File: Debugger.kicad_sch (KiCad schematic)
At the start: 32 parts, among them IC1 STM32F103C8T6, J1 USB_B_Micro, J2 Conn_01x06_Pin, Q4 MMBT3904, SW1 RESET, U4 USBLC6-2SC6, Y1 8MHz

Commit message: update
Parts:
- SW1: value RESET -> SW_Push
- renumbered IC1 to U6
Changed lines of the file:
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@@
 		(on_board yes)
 		(dnp no)
-		(property "Reference" "IC1"
+		(property "Reference" "U6"
 			(at 124.968 102.362 0)
 			(effects
@@
 			(project ""
 				(path "/c703575f-b97a-4282-ae81-d5777b8a5a01/7972b3b3-0781-42c8-aedd-35cecbf74189"
-					(reference "IC1")
+					(reference "U6")
 					(unit 1)
 				)
@@
 			)
 		)
-		(property "Value" "RESET"
+		(property "Value" "SW_Push"
 			(at 237.49 48.2599 90)
 			(effects

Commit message: Done ERC + Documentation
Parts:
- removed Q4: MMBT3904, Package_TO_SOT_SMD:SOT-23, symbol Simulation_SPICE:NPN
- removed R45: 36k, Resistor_SMD:R_0603_1608Metric, symbol Device:R_US
- removed R46: 100k, Resistor_SMD:R_0603_1608Metric, symbol Device:R_US
- added R23, R24: 22R, Resistor_SMD:R_0603_1608Metric, symbol Device:R_US
- U3: renamed from U6; footprint QFP50P900X900X160-48N -> footprints:QFP50P900X900X160-48N; MPN (none) -> STM32F103C8T6; Manufacturer_Part_Number STM32F103C8T6 -> (none)
- U4: MPN (none) -> USBLC6-2SC6
- renumbered C1 to C21, C2 to C22, C3 to C23, C4 to C24, C5 to C25, C6 to C26, C7 to C27, C8 to C28, C9 to C29, C10 to C30, D1 to D6, D2 to D7, J2 to J4, J1 to J5, R1 to R15, R2 to R16, R3 to R17, R4 to R18, R5 to R19, R6 to R20, R7 to R21, R8 to R22, R9 to R25, R44 to R26, R10 to R27, SW1 to SW5
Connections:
- net +3.3V: now also R26.1
- net USB_DN: now also R24.1; no longer U4.3 (I/O2)
- net USB_DP: now also R23.2; no longer R26.2, U4.1 (I/O1)
- net T_NRST renamed RESET
- new net: R23.1, R26.2, U4.1 (I/O1)
- new net: R24.2, U4.3 (I/O2)
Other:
- moved on the sheet: D7, J5, R26, R27, U4

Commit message: Initial Review Changes
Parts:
- added F1: Polyfuse, Fuse:Fuse_1206_3216Metric, symbol Device:Polyfuse
- J4: value Conn_01x06_Pin -> F103 SWD
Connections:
- net at D7.2 (A), U4.5 (VBUS): now also F1.1; no longer J5.1 (VBUS)
- new net: F1.2, J5.1 (VBUS)
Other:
- company: (none) -> _electronic_projects
- title: (none) -> DeskNode-F4
- moved on the sheet: J5
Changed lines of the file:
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@@
 	(generator_version "9.0")
 	(paper "A4")
+	(title_block
+		(title "DeskNode-F4")
+		(rev "A")
+		(company "_electronic_projects")
+		(comment 1 "Wajahatulla Sharif")
+		(comment 2 "Designed by ")
+	)
 	(rectangle
 		(start 218.186 125.73)
@@
 	)
 	(junction
-		(at 254 95.25)
+		(at 69.85 114.3)
 		(diameter 0)
 		(color 0 0 0 0)
 	)
 	(junction
-		(at 69.85 114.3)
+		(at 270.51 114.3)
 		(diameter 0)
 		(color 0 0 0 0)
@@
 	)
 	(junction
-		(at 267.97 114.3)
-		(diameter 0)
-		(color 0 0 0 0)
-	)
-	(junction
 		(at 257.81 114.3)
 		(diameter 0)
@@
 	)
 	(junction
+		(at 254 95.25)
+		(diameter 0)
+		(color 0 0 0 0)
+	)
+	(junction
 		(at 78.74 48.26)
 		(diameter 0)
@@
 	(wire
 		(pts
-			(xy 254 95.25) (xy 260.35 95.25)
-		)
-		(stroke
-			(width 0)
-			(type default)
-		)
-	)
-	(wire
-		(pts
-			(xy 259.08 100.33) (xy 260.35 100.33)
+			(xy 259.08 100.33) (xy 262.89 100.33)
 		)
 		(stroke
@@
 	(wire
 		(pts
-			(xy 259.08 102.87) (xy 260.35 102.87)
+			(xy 259.08 102.87) (xy 262.89 102.87)
 		)
 		(stroke
@@
 	(wire
 		(pts
-			(xy 270.51 114.3) (xy 267.97 114.3)
+			(xy 273.05 114.3) (xy 270.51 114.3)
 		)
 		(stroke
@@
 	(wire
 		(pts
-			(xy 260.35 105.41) (xy 257.81 105.41)
+			(xy 262.89 105.41) (xy 257.81 105.41)
 		)
 		(stroke
@@
 	(wire
 		(pts
-			(xy 257.81 114.3) (xy 267.97 114.3)
+			(xy 257.81 114.3) (xy 270.51 114.3)
 		)
 		(stroke
@@
 	(wire
 		(pts
-			(xy 267.97 110.49) (xy 267.97 114.3)
+			(xy 270.51 110.49) (xy 270.51 114.3)
 		)
 		(stroke
@@
 	(wire
 		(pts
+			(xy 255.27 95.25) (xy 254 95.25)
+		)
+		(stroke
+			(width 0)
+			(type default)
+		)
+	)
+	(wire
+		(pts
 			(xy 163.83 88.9) (xy 163.83 81.28)
 		)
@@
 	(wire
 		(pts
-			(xy 270.51 110.49) (xy 270.51 114.3)
+			(xy 273.05 110.49) (xy 273.05 114.3)
 		)
 		(stroke
@@
 		(dnp no)
 		(property "Reference" "J4"
-			(at 259.715 135.89 0)
+			(at 259.842 134.874 0)
 			(effects
 				(font
@@
 			)
 		)
-		(property "Value" "Conn_01x06_Pin"
-			(at 259.715 138.43 0)
+		(property "Value" "F103 SWD"
+			(at 259.842 137.414 0)
 			(effects
 				(font
@@
 	)
 	(symbol
+		(lib_id "Device:Polyfuse")
+		(at 259.08 95.25 90)
+		(unit 1)
+		(exclude_from_sim no)
+		(in_bom yes)
+		(on_board yes)
+		(dnp no)
+		(fields_autoplaced yes)
+		(property "Reference" "F1"
+			(at 259.08 88.9 90)
+			(effects
+				(font
+					(size 1.27 1.27)
+				)
+			)
+		)
+		(property "Value" "Polyfuse"
+			(at 259.08 91.44 90)
+			(effects
+				(font
+					(size 1.27 1.27)
+				)
+			)
+		)
+		(property "Footprint" "Fuse:Fuse_1206_3216Metric"
+			(at 264.16 93.98 0)
+			(effects
+				(font
+					(size 1.27 1.27)
+				)
+				(justify left)
+				(hide yes)
+			)
+		)
+		(property "Datasheet" "~"
+			(at 259.08 95.25 0)
+			(effects
+				(font
+					(size 1.27 1.27)
+				)
+				(hide yes)
+			)
+		)
+		(property "Description" "Resettable fuse, polymeric positive temperature coefficient"
+			(at 259.08 95.25 0)
+			(effects
+				(font
+					(size 1.27 1.27)
+				)
+				(hide yes)
+			)
+		)
+		(property "MPN" "NANOSMDC075F-2"
+			(at 259.08 95.25 90)
+			(effects
+				(font
+					(size 1.27 1.27)
+				)
+				(hide yes)
+			)
+		)
+		(property "Manufacturer" "Littlefuse"
+			(at 259.08 95.25 90)
+			(effects
+				(font
+					(size 1.27 1.27)
+				)
+				(hide yes)
+			)
+		)
+		(pin "2"
+		)
+		(pin "1"
+		)
+		(instances
+			(project "STM32 Microcontroller Board"
+				(path "/c703575f-b97a-4282-ae81-d5777b8a5a01/7972b3b3-0781-42c8-aedd-35cecbf74189"
+					(reference "F1")
+					(unit 1)
+				)
+			)
+		)
+	)
+	(symbol
 		(lib_id "Device:R_US")
 		(at 173.99 110.49 90)
@@
 	(symbol
 		(lib_id "Connector:USB_B_Micro")
-		(at 267.97 100.33 0)
+		(at 270.51 100.33 0)
 		(mirror y)
 		(unit 1)
@@
 		(dnp no)
 		(property "Reference" "J5"
-			(at 267.97 87.63 0)
+			(at 270.51 87.63 0)
 			(effects
 				(font
@@
 		)
 		(property "Value" "USB_B_Micro"
-			(at 267.97 90.17 0)
+			(at 270.51 90.17 0)
 			(effects
 				(font
@@
 		)
 		(property "Footprint" "Connector_USB:USB_Micro-B_GCT_USB3076-30-A"
-			(at 264.16 101.6 0)
+			(at 266.7 101.6 0)
 			(effects
 				(font
@@
 		)
 		(property "Datasheet" "~"
-			(at 264.16 101.6 0)
+			(at 266.7 101.6 0)
 			(effects
 				(font
@@
 		)
 		(property "Description" "USB Micro Type B connector"
-			(at 267.97 100.33 0)
+			(at 270.51 100.33 0)
 			(effects
 				(font
@@
 		)
 		(property "MPN" "USB3076-30-A"
-			(at 267.97 100.33 0)
+			(at 270.51 100.33 0)
 			(effects
 				(font

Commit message: MPNs updated
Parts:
- C21, C22: value 30pF -> 27pF; footprint Capacitor_SMD:C_0805_2012Metric -> Capacitor_SMD:C_0603_1608Metric; MPN (none) -> CL10C270JB8NNNC
- J5: footprint Connector_USB:USB_Micro-B_GCT_USB3076-30-A -> footprints:USB_Micro-B_GCT_USB3076-30-A
- R15, R16: MPN (none) -> RC0603FR-074K7L
- R17, R18, R19, R20, R27: MPN (none) -> RC0603FR-07100KL
- R21, R22: value 220 -> 680R; MPN (none) -> RC0603FR-07680RL
- R23, R24: MPN (none) -> RC0603FR-0722RL
- R25: MPN (none) -> RC0603FR-0710KL
- R26: MPN (none) -> RC0603FR-071K5L

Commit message: Layout placement
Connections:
- net T_SWDIO: now also U3.27 (PB14); no longer U3.25 (PB12)
- net TX: now reaches U3.12 (PA2)
- net RX: now reaches U3.13 (PA3)
- no-connect marks 21 -> 19
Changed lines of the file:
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@@
 	)
 	(no_connect
-		(at 96.52 114.3)
-	)
-	(no_connect
 		(at 130.81 127)
 	)
@@
 	)
 	(no_connect
-		(at 110.49 127)
-	)
-	(no_connect
 		(at 120.65 127)
 	)
@@
 	)
 	(no_connect
-		(at 156.21 109.22)
-	)
-	(no_connect
 		(at 96.52 93.98)
 	)
@@
 	)
 	(no_connect
+		(at 156.21 114.3)
+	)
+	(no_connect
 		(at 133.35 127)
 	)
@@
 	(wire
 		(pts
-			(xy 154.94 114.3) (xy 152.4 114.3)
+			(xy 156.21 114.3) (xy 152.4 114.3)
 		)
 		(stroke
@@
 	(wire
 		(pts
+			(xy 110.49 128.27) (xy 110.49 127)
+		)
+		(stroke
+			(width 0)
+			(type default)
+		)
+	)
+	(wire
+		(pts
 			(xy 247.65 154.94) (xy 247.65 153.67)
 		)
@@
 	(wire
 		(pts
+			(xy 95.25 114.3) (xy 96.52 114.3)
+		)
+		(stroke
+			(width 0)
+			(type default)
+		)
+	)
+	(wire
+		(pts
 			(xy 63.5 99.06) (xy 63.5 106.68)
 		)
@@
 	(wire
 		(pts
-			(xy 152.4 109.22) (xy 156.21 109.22)
+			(xy 152.4 109.22) (xy 154.94 109.22)
 		)
 		(stroke
@@
 		)
 	)
+	(hierarchical_label "TX"
+		(shape bidirectional)
+		(at 95.25 114.3 180)
+		(effects
+			(font
+				(size 1.27 1.27)
+			)
+			(justify right)
+		)
+	)
 	(hierarchical_label "T_SWDIO"
 		(shape bidirectional)
-		(at 154.94 114.3 0)
+		(at 154.94 109.22 0)
 		(effects
 			(font
@@
 		)
 	)
+	(hierarchical_label "RX"
+		(shape bidirectional)
+		(at 110.49 128.27 270)
+		(effects
+			(font
+				(size 1.27 1.27)
+			)
+			(justify right)
+		)
+	)
 	(symbol
 		(lib_id "power:GND")
@@
 		(on_board yes)
 		(dnp no)
-		(fields_autoplaced yes)
 		(property "Reference" "F1"
-			(at 259.08 88.9 90)
+			(at 259.08 88.392 90)
 			(effects
 				(font
@@
 		)
 		(property "Value" "Polyfuse"
-			(at 259.08 91.44 90)
+			(at 259.08 90.932 90)
 			(effects
 				(font
@@
 		)
 		(property "MPN" "NANOSMDC075F-2"
-			(at 259.08 95.25 90)
+			(at 259.08 92.964 90)
 			(effects
 				(font
-					(size 1.27 1.27)
+					(size 0.889 0.889)
 				)
-				(hide yes)
 			)
 		)
@@
 		(on_board yes)
 		(dnp no)
-		(fields_autoplaced yes)
 		(property "Reference" "Y1"
 			(at 54.61 96.5199 90)
@@
 		)
 		(property "MPN" "ECS-80-18-5PX-TR"
-			(at 50.8 97.79 90)
+			(at 52.324 93.726 90)
 			(effects
 				(font
 					(size 1.27 1.27)
 				)
-				(hide yes)
 			)
 		)
@@
 		(dnp no)
 		(property "Reference" "J5"
-			(at 270.51 87.63 0)
+			(at 270.51 86.36 0)
 			(effects
 				(font
@@
 		)
 		(property "Value" "USB_B_Micro"
-			(at 270.51 90.17 0)
+			(at 270.51 88.9 0)
 			(effects
 				(font
@@
 		)
 		(property "MPN" "USB3076-30-A"
-			(at 270.51 100.33 0)
+			(at 270.764 91.186 0)
 			(effects
 				(font
-					(size 1.27 1.27)
+					(size 0.889 0.889)
 				)
-				(hide yes)
 			)
 		)

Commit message: Layout Routing
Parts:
- F1: MPN NANOSMDC075F-2 -> NANOSMDC075
- J5: MPN USB3076-30-A -> USB3076-30
- U4: value USBLC6-2SC6 -> USBLC6-2
- Y1: MPN ECS-80-18-5PX-TR -> ECS80185PX
- renumbered C21 to C22, C22 to C23, C23 to C24, C24 to C25, C25 to C26, C26 to C27, C27 to C28, C28 to C29, C29 to C30, C30 to C31, D6 to D7, D7 to D8
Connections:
- net at D8.2 (A), F1.1: no longer U4.5 (VBUS)
- net at F1.2, J5.1 (VBUS): now also U4.5 (VBUS)
- net USB_DN renamed USB_N
- net USB_DP renamed USB_P
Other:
- moved on the sheet: D8, F1, R23, R24, R26, R27, U4

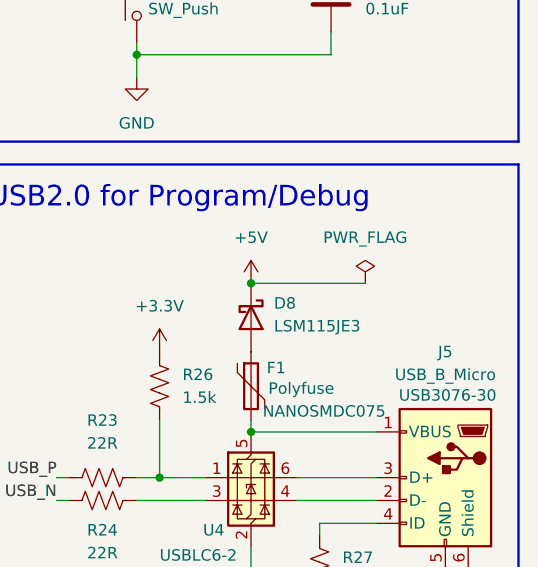
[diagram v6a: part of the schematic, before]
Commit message: Layout - 12V Power path
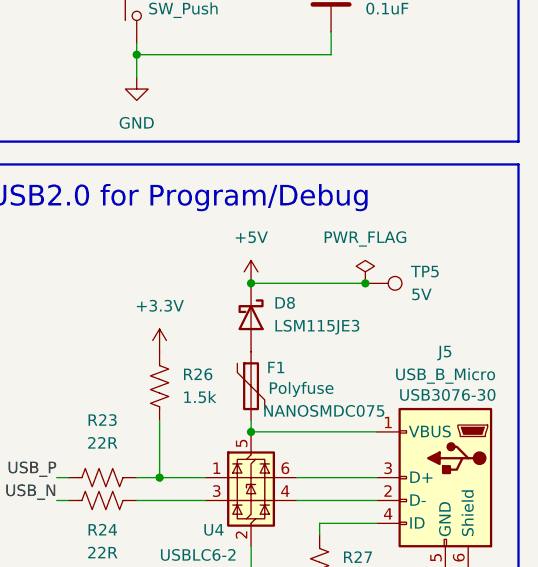
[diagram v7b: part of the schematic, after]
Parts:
- added TP5: 5V, TestPoint:TestPoint_Keystone_5000-5004_Miniature, symbol Connector:TestPoint
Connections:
- net +5V: now also TP5.1
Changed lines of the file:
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@@
+	)
+	(junction
+		(at 261.62 78.74)
+		(diameter 0)
+		(color 0 0 0 0)
 	)
 	(junction
@@
 					(unit 1)
 				)
+			)
+		)
+	)
+	(symbol
+		(lib_id "Connector:TestPoint")
+		(at 261.62 78.74 270)
+		(unit 1)
+		(exclude_from_sim no)
+		(in_bom yes)
+		(on_board yes)
+		(dnp no)
+		(fields_autoplaced yes)
+		(property "Reference" "TP5"
+			(at 266.7 77.4699 90)
+			(effects
+				(font
+					(size 1.27 1.27)
+				)
+				(justify left)
+			)
+		)
+		(property "Value" "5V"
+			(at 266.7 80.0099 90)
+			(effects
+				(font
+					(size 1.27 1.27)
+				)
+				(justify left)
+			)
+		)
+		(property "Footprint" "TestPoint:TestPoint_Keystone_5000-5004_Miniature"
+			(at 261.62 83.82 0)
+			(effects
+				(font
+					(size 1.27 1.27)
+				)
+				(hide yes)
+			)
+		)
+		(property "Datasheet" "~"
+			(at 261.62 83.82 0)
+			(effects
+				(font
+					(size 1.27 1.27)
+				)
+				(hide yes)
+			)
+		)
+		(property "Description" "test point"
+			(at 261.62 78.74 0)
+			(effects
+				(font
+					(size 1.27 1.27)
+				)
+				(hide yes)
+			)
+		)
+		(property "MPN" "5001"
+			(at 261.62 78.74 90)
+			(effects
+				(font
+					(size 1.27 1.27)
+				)
+				(hide yes)
+			)
+		)
+		(property "Manufacturer_Part_Number" ""
+			(at 261.62 78.74 90)
+			(effects
+				(font
+					(size 1.27 1.27)
+				)
+				(hide yes)
+			)
+		)
+		(pin "1"
+		)
+		(instances
+			(project "STM32 Microcontroller Board"
+				(path "/c703575f-b97a-4282-ae81-d5777b8a5a01/7972b3b3-0781-42c8-aedd-35cecbf74189"
+					(reference "TP5")
+					(unit 1)
+				)

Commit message: Review files
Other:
- company: _electronic_projects -> (none)
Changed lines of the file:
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@@
 		(title "DeskNode-F4")
 		(rev "A")
-		(company "_electronic_projects")
-		(comment 1 "Wajahatulla Sharif")
-		(comment 2 "Designed by ")
 	)
 	(rectangle
